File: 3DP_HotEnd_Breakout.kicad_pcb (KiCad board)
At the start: 2 copper layers, 47.4 x 23.5 mm, 21 parts, among them J1 Conn_01x02_Male, J11 Conn_01x02, J11 Conn_01x02_Male, J12 Conn_01x02_Male, J13 Conn_01x02, J2 Conn_01x02, J3 Conn_01x02, J4 Conn_01x02, J5 Conn_01x02_Male, J6 1751248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

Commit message: REV1
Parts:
- removed the J11 at (109.2, 62.2)
- removed the J11 at (109.2, 68.6)
- added H1: MountingHole, MountingHole:MountingHole_3.2mm_M3, F.Cu at (-21.0, -8.75)
- added H2: MountingHole, MountingHole:MountingHole_3.2mm_M3, F.Cu at (21.0, 8.75)
- added H3: MountingHole, MountingHole:MountingHole_3.2mm_M3, F.Cu at (21.0, -8.75)
- added H4: MountingHole, MountingHole:MountingHole_3.2mm_M3, F.Cu at (-21.0, 8.75)
- added J10: Conn_01x02_Male, Connector_PinHeader_2.54mm:PinHeader_1x02_P2.54mm_Vertical, F.Cu at (-5.75, -3.25)
- added J11: Conn_01x02, 3DP_HotEnd_Breakout:JST_XH_B2B-XH-AM_1x02_P2.50mm_Vertical_DJP, F.Cu at (-5.00, -9.00)
- added J14: Conn_01x02_Male, Connector_PinHeader_2.54mm:PinHeader_1x02_P2.54mm_Vertical, F.Cu at (-6.00, 0.50)
- added J15: Conn_01x02_Male, Connector_PinHeader_2.54mm:PinHeader_1x02_P2.54mm_Vertical, F.Cu at (-2.25, 0.50)
- D1, D2, D3, D4: footprint LED_SMD:LED_0805_2012Metric_Pad1.15x1.40mm_HandSolder -> 3DP_HotEnd_Breakout:LED_0805_2012Metric_Pad1.15x1.40mm_HandSolder
- J13, J2, J3, J4: footprint CArraigeFanBreakout:JST_XH_B2B-XH-AM_1x02_P2.50mm_Vertical_DJP -> 3DP_HotEnd_Breakout:JST_XH_B2B-XH-AM_1x02_P2.50mm_Vertical_DJP
- J6, J7: footprint CArraigeFanBreakout:Phoenix_Contact-1751248-0-0-0 -> 3DP_HotEnd_Breakout:Phoenix_Contact-1751248-0-0-0
- moved J8 139.4 mm to (-9.75, 6.41)
- moved D1 139.2 mm to (13.0, -10.5), turned to 180 degrees
- moved R1 139.2 mm to (13.5, -8.50), turned to 0 degrees
- moved J2 134.1 mm to (4.50, -9.01)
- moved J6 134.0 mm to (-11.9, -8.26)
- moved J7 134.0 mm to (-11.9, -0.28)
- moved J12 133.9 mm to (-21.7, 3.52)
- moved J13 133.8 mm to (-21.5, -2.29)
- moved J4 133.7 mm to (6.75, 8.75)
- moved J1 133.6 mm to (5.50, -3.25)
- moved J9 133.5 mm to (-9.75, 10.0)
- moved J3 133.4 mm to (-1.75, 8.75)
- moved D2 133.1 mm to (13.0, 10.5)
- moved R2 132.6 mm to (13.2, 8.50), turned to 180 degrees
- moved J5 132.5 mm to (7.75, 3.00)
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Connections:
- D1 pad 1: +FAN0 -> Net-(D1-Pad1)
- D1 pad 2: Net-(D1-Pad2) -> +FAN0
- D2 pad 1: +FAN1 -> -FAN1
- D3 pad 1: +V_LED -> -V_LED
- D4 pad 1: +V_IN -> -V_IN
- J1 pad 1: -FAN0 -> +FAN0
- J1 pad 2: +FAN0 -> -FAN0
- J2 pad 1: -FAN0 -> +FAN0
- J2 pad 2: +FAN0 -> -FAN0
- J3 pad 1: -FAN1 -> +FAN1
- J3 pad 2: +FAN1 -> -FAN1
- J4 pad 1: -FAN1 -> +FAN1
- J4 pad 2: +FAN1 -> -FAN1
- J5 pad 1: -FAN1 -> +FAN1
- J5 pad 2: +FAN1 -> -FAN1
- J6 pad 1: -V_IN -> +V_IN
- J6 pad 2: +V_IN -> -V_IN
- R1 pad 1: Net-(D1-Pad2) -> -FAN0
- R1 pad 2: -FAN0 -> Net-(D1-Pad1)
- R2 pad 2: -FAN1 -> +FAN1
- R3 pad 2: -V_LED -> +V_LED
- R4 pad 2: -V_IN -> +V_IN
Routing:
- net +V_LED: track 16.5 -> 70.9 mm, vias 0 -> 1
- net +V_IN: track 41.1 -> 84.4 mm, vias 0 -> 1
- net -V_IN: track 56.7 -> 91.8 mm, vias 0 -> 1
- net -V_LED: track 22.8 -> 53.7 mm, vias 0 -> 1
- net -FAN1: track 43.8 -> 65.6 mm, vias 0 -> 1
- net -V_Probe: track 27.9 -> 7.17 mm
- net +3V3: track 27.0 -> 7.17 mm
- net Z_PROBE_CONN: track 25.6 -> 7.17 mm
- net +FAN0: track 18.5 -> 30.6 mm, vias 0 -> 1
- net Net-(J14-Pad2): track 0.00 -> 7.50 mm
- net Net-(J14-Pad1): track 0.00 -> 7.50 mm
- net +FAN1: track 49.2 -> 42.3 mm, vias 0 -> 1
- net Net-(D1-Pad2): track 2.67 -> 0.00 mm
- net Net-(D1-Pad1): track 0.00 -> 2.16 mm
- net Net-(D3-Pad2): track 2.17 -> 4.11 mm
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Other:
- board size 47.4 x 23.5 mm -> 49 x 24.5 mm
- board text added: "AUX1"
- board text added: "E0"
- board text added: "FAN0"
- board text added: "FAN1"
- board text added: "LED"
- board text added: "THERM"

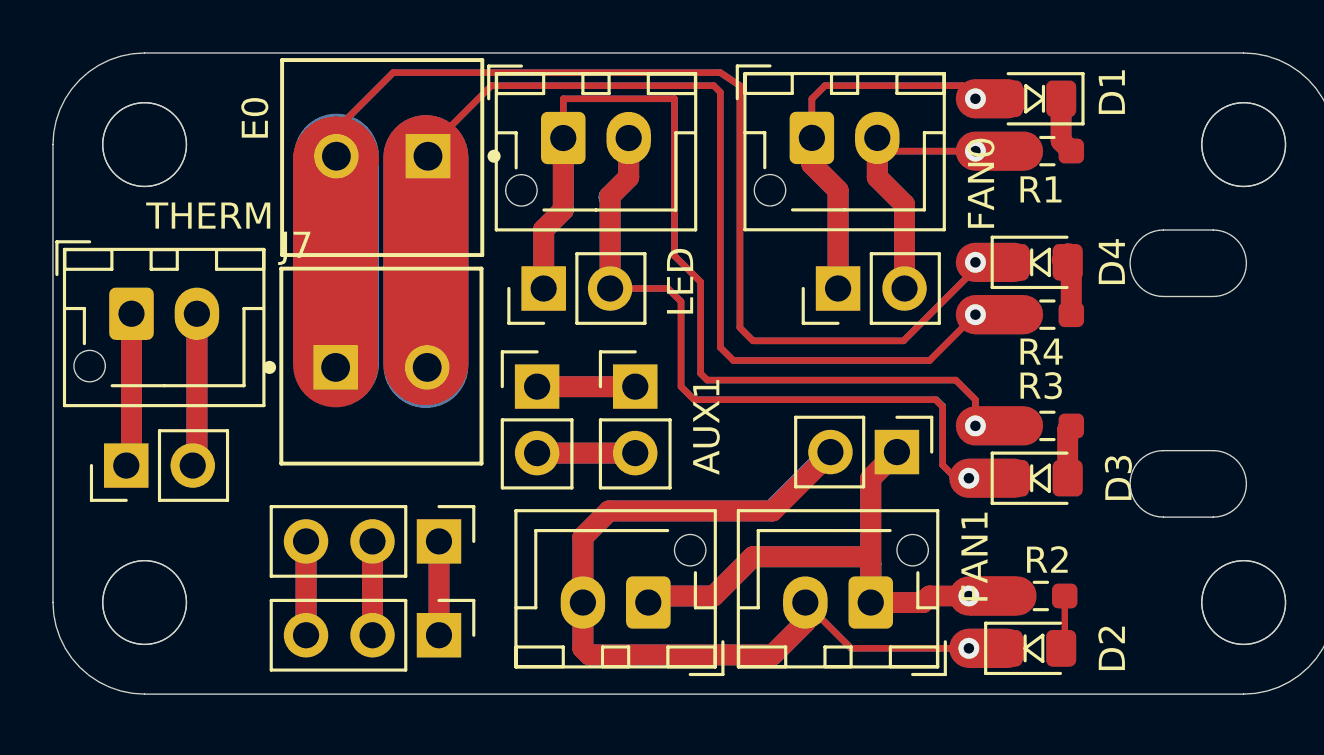
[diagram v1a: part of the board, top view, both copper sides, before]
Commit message: revised SMT pads
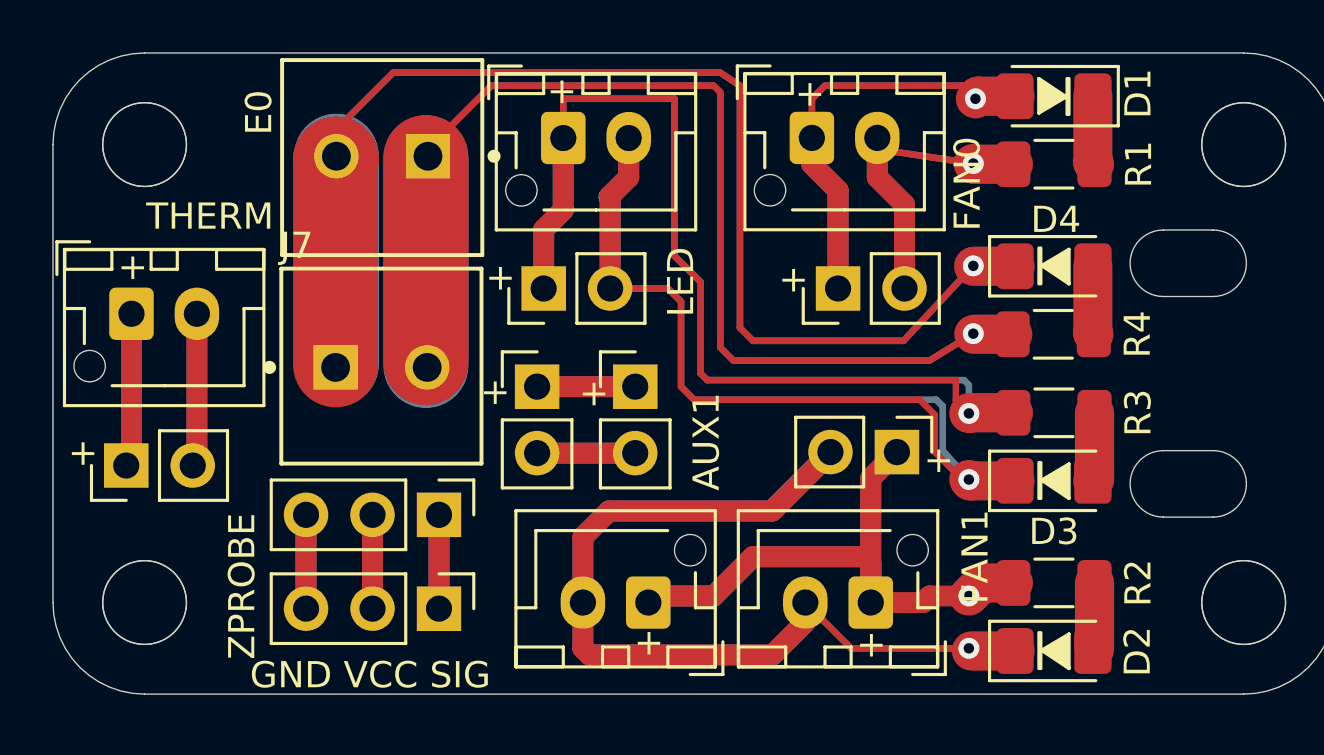
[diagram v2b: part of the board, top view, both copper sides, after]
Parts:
- D1, D2, D3, D4: footprint 3DP_HotEnd_Breakout:LED_0805_2012Metric_Pad1.15x1.40mm_HandSolder -> 3DP_HotEnd_Breakout:LED_1206_3216Metric_Pad1.42x1.75mm_HandSolder
- R1, R2, R3, R4: footprint Resistor_SMD:R_0603_1608Metric_Pad0.98x0.95mm_HandSolder -> Resistor_SMD:R_1206_3216Metric_Pad1.30x1.75mm_HandSolder
- moved J8 1.02 mm to (-9.75, 5.40)
- moved J9 1.02 mm to (-9.75, 8.98)
- moved R4 0.78 mm to (13.7, -1.50)
- moved D1 0.76 mm to (13.8, -10.6)
- moved D2 0.76 mm to (13.8, 10.6)
- moved R2 0.71 mm to (13.8, 8.00)
- moved R1 0.56 mm to (13.8, -8.00)
- moved R3 0.56 mm to (13.8, 1.50)
- moved D4 0.52 mm to (13.8, -4.10)
- moved D3 0.51 mm to (13.8, 4.10)
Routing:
- net Net-(D4-Pad2): track 4.45 -> 2.67 mm
- net Net-(D3-Pad2): track 4.11 -> 2.71 mm
- net +V_IN: track 84.4 -> 83.0 mm
- net +V_LED: track 70.9 -> 69.8 mm
- net -FAN0: track 22.4 -> 21.7 mm
- net Net-(D1-Pad1): track 2.16 -> 2.78 mm
- net Net-(D2-Pad2): track 2.06 -> 2.63 mm
- net -V_LED: track 53.7 -> 53.2 mm
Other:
- board text added: "+"
- board text added: "GND VCC SIG"
- board text added: "SIG VCC GDN"
- board text added: "ZPROBE"
